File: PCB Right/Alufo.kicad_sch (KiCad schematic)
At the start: 32 parts, among them J2 USB_C_Receptacle_USB2.0_16P_2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, J4 USB_C_Receptacle_USB2.0_16P_2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, J6 SolderHole, SW2 BOOT, U2 CH552T, U4 USBLC6-2P6, U6 USBLC6-2P6

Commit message: Add cutout in middle layer for solder jump
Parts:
- J6: footprint TestPoint:TestPoint_THTPad_D2.5mm_Drill1.2mm -> Project Library:TestPoint_THTPad_D2.5mm_Drill1.2mm
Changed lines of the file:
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@@
 			)
 		)
-		(property "Footprint" "TestPoint:TestPoint_THTPad_D2.5mm_Drill1.2mm"
+		(property "Footprint" "Project Library:TestPoint_THTPad_D2.5mm_Drill1.2mm"
 			(at 165.1 157.48 0)
 			(effects

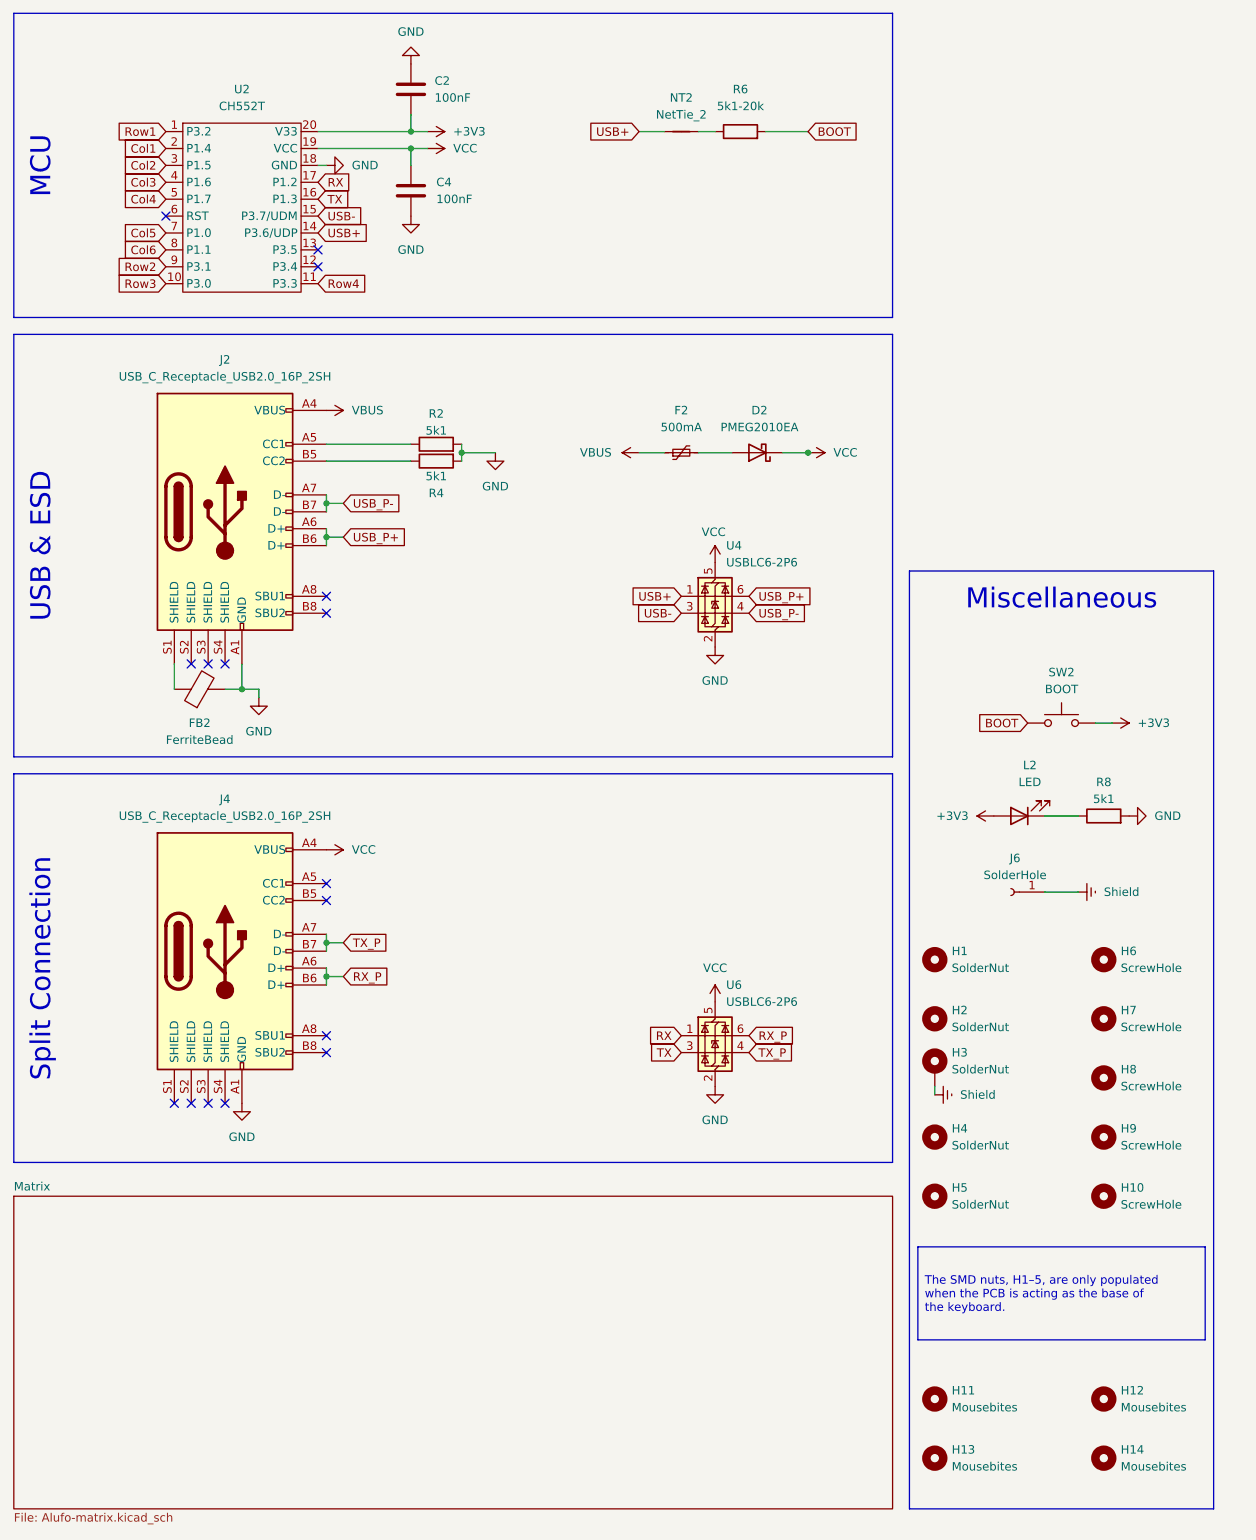
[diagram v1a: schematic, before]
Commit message: Update to KiCad v9
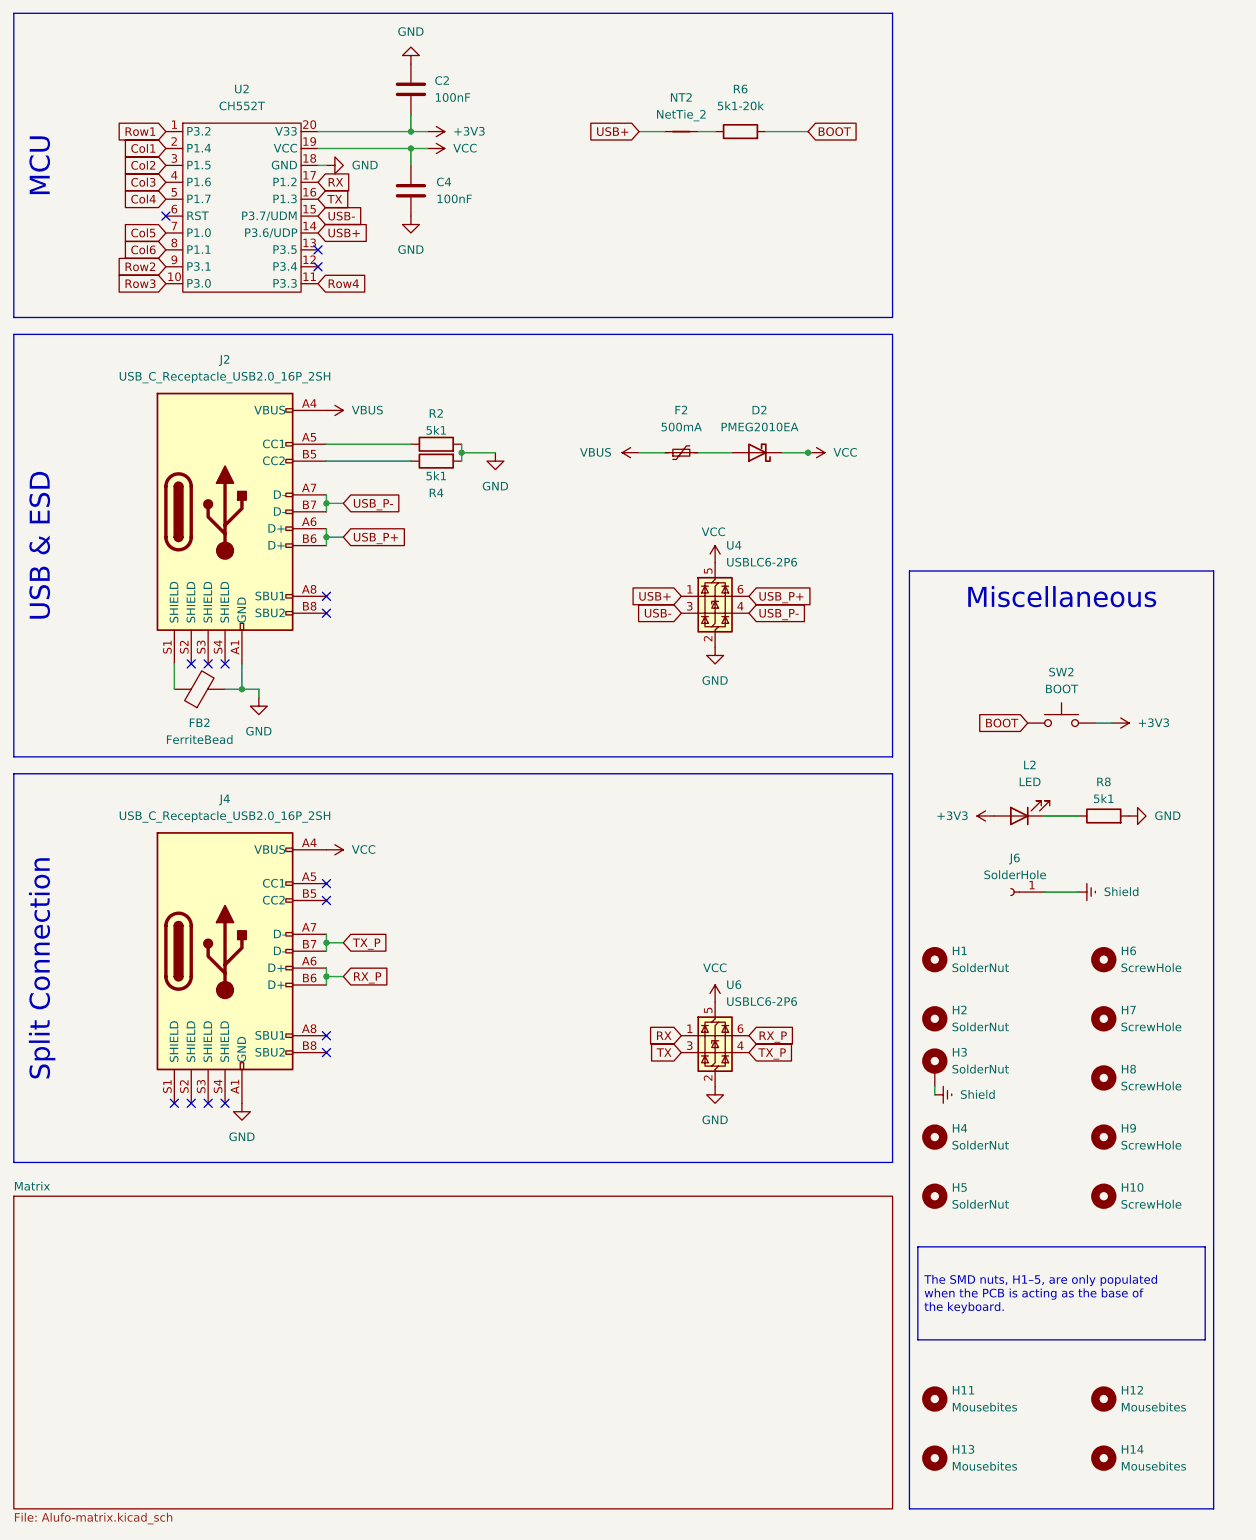
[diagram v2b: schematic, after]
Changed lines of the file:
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@@
 (kicad_sch
-	(version 20231120)
+	(version 20250114)
 	(generator "eeschema")
-	(generator_version "8.0")
+	(generator_version "9.0")
 	(paper "A4" portrait)
 	(title_block
@@
 		(comment 1 "Split one-layer reversible keyboard PCB (righthand side)")
 	)
+	(text_box "MCU"
+		(exclude_from_sim no)
+		(at 15.24 25.4 90)
+		(size 132.08 45.72)
+		(margins 2.25 2.25 2.25 2.25)
+		(stroke
+			(width 0)
+			(type default)
+		)
+		(fill
+			(type none)
+		)
+		(effects
+			(font
+				(size 3 3)
+			)
+			(justify top)
+		)
+	)
+	(text_box "Miscellaneous"
+		(exclude_from_sim no)
+		(at 149.86 109.22 0)
+		(size 45.72 140.97)
+		(margins 2.25 2.25 2.25 2.25)
+		(stroke
+			(width 0)
+			(type default)
+		)
+		(fill
+			(type none)
+		)
+		(effects
+			(font
+				(size 3 3)
+			)
+			(justify top)
+		)
+	)
+	(text_box "Split Connection"
+		(exclude_from_sim no)
+		(at 15.24 139.7 90)
+		(size 132.08 58.42)
+		(margins 2.25 2.25 2.25 2.25)
+		(stroke
+			(width 0)
+			(type default)
+		)
+		(fill
+			(type none)
+		)
+		(effects
+			(font
+				(size 3 3)
+			)
+			(justify top)
+		)
+	)
+	(text_box "USB & ESD"
+		(exclude_from_sim no)
+		(at 15.24 73.66 90)
+		(size 132.08 63.5)
+		(margins 2.25 2.25 2.25 2.25)
+		(stroke
+			(width 0)
+			(type default)
+		)
+		(fill
+			(type none)
+		)
+		(effects
+			(font
+				(size 3 3)
+			)
+			(justify top)
+		)
+	)
+	(text_box "The SMD nuts, H1–5, are only populated when the PCB is acting as the base of the keyboard."
+		(exclude_from_sim no)
+		(at 151.13 210.82 0)
+		(size 43.18 13.97)
+		(margins 0.9525 0.9525 0.9525 0.9525)
+		(stroke
+			(width 0)
+			(type default)
+		)
+		(fill
+			(type none)
+		)
+		(effects
+			(font
+				(size 1.27 1.27)
+			)
+			(justify left)
+		)
+	)
 	(junction
 		(at 49.53 127)
@@
 		)
 	)
-	(text_box "MCU"
-		(exclude_from_sim no)
-		(at 15.24 25.4 90)
-		(size 132.08 45.72)
-		(stroke
-			(width 0)
-			(type default)
-		)
-		(fill
-			(type none)
-		)
-		(effects
-			(font
-				(size 3 3)
-			)
-			(justify top)
-		)
-	)
-	(text_box "Miscellaneous"
-		(exclude_from_sim no)
-		(at 149.86 109.22 0)
-		(size 45.72 140.97)
-		(stroke
-			(width 0)
-			(type default)
-		)
-		(fill
-			(type none)
-		)
-		(effects
-			(font
-				(size 3 3)
-			)
-			(justify top)
-		)
-	)
-	(text_box "Split Connection"
-		(exclude_from_sim no)
-		(at 15.24 139.7 90)
-		(size 132.08 58.42)
-		(stroke
-			(width 0)
-			(type default)
-		)
-		(fill
-			(type none)
-		)
-		(effects
-			(font
-				(size 3 3)
-			)
-			(justify top)
-		)
-	)
-	(text_box "USB & ESD"
-		(exclude_from_sim no)
-		(at 15.24 73.66 90)
-		(size 132.08 63.5)
-		(stroke
-			(width 0)
-			(type default)
-		)
-		(fill
-			(type none)
-		)
-		(effects
-			(font
-				(size 3 3)
-			)
-			(justify top)
-		)
-	)
-	(text_box "The SMD nuts, H1–5, are only populated when the PCB is acting as the base of the keyboard."
-		(exclude_from_sim no)
-		(at 151.13 210.82 0)
-		(size 43.18 13.97)
-		(stroke
-			(width 0)
-			(type default)
-		)
-		(fill
-			(type none)
-		)
-		(effects
-			(font
-				(size 1.27 1.27)
-			)
-			(justify left)
-		)
-	)
 	(global_label "USB-"
 		(shape input)
@@
 		(at 15.24 203.2)
 		(size 132.08 46.99)
+		(exclude_from_sim no)
+		(in_bom yes)
+		(on_board yes)
+		(dnp no)
 		(fields_autoplaced yes)
 		(stroke
@@
 		)
 	)
+	(embedded_fonts no)
 )

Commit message: Further library name corrections in schematic; update PCB
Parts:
- H1, H2, H4, H5: footprint Project Library:MountingHole_2.2mm_M2_SMD_Solder_Nut -> Project_Library:MountingHole_2.2mm_M2_SMD_Solder_Nut
- H11, H12, H13, H14: footprint Project Library:Mousebites -> Project_Library:Mousebites
- H3: footprint Project Library:MountingHole_2.2mm_M2_SMD_Solder_Nut_Pad -> Project_Library:MountingHole_2.2mm_M2_SMD_Solder_Nut_Pad
- J2, J4: footprint Project Library:USB_C_Receptacle_HRO_TYPE-C-31-M-12 -> Project_Library:USB_C_Receptacle_HRO_TYPE-C-31-M-12; symbol Project Library:USB_C_Receptacle_USB2.0_16P_2SH -> Project_Library:USB_C_Receptacle_USB2.0_16P_2SH
- J6: footprint Project Library:TestPoint_THTPad_D2.5mm_Drill1.2mm -> Project_Library:TestPoint_THTPad_D2.5mm_Drill1.2mm
- L2: footprint Project Library:LED_0805_2012Metric_Mod -> Project_Library:LED_0805_2012Metric_Mod
- NT2: footprint Project Library:NetTie-2_SMD_Pad0.2mm -> Project_Library:NetTie-2_SMD_Pad0.2mm
- SW2: footprint Project Library:SW_SPST_SKQG_WithStem -> Project_Library:SW_SPST_SKQG_WithStem
- U2: symbol Project Library:MCU_CH552T_TSSOP-20 -> Project_Library:MCU_CH552T_TSSOP-20
- U4, U6: footprint Project Library:SOT-666_Mod -> Project_Library:SOT-666_Mod
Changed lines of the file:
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@@
 	)
 	(symbol
-		(lib_id "Project Library:USB_C_Receptacle_USB2.0_16P_2SH")
+		(lib_id "Project_Library:USB_C_Receptacle_USB2.0_16P_2SH")
 		(at 46.99 100.33 0)
 		(unit 1)
@@
 			)
 		)
-		(property "Footprint" "Project Library:USB_C_Receptacle_HRO_TYPE-C-31-M-12"
+		(property "Footprint" "Project_Library:USB_C_Receptacle_HRO_TYPE-C-31-M-12"
 			(at 50.8 100.33 0)
 			(effects
@@
 			)
 		)
-		(property "Footprint" "Project Library:Mousebites"
+		(property "Footprint" "Project_Library:Mousebites"
 			(at 179.07 233.68 0)
 			(effects
@@
 	)
 	(symbol
-		(lib_id "Project Library:USB_C_Receptacle_USB2.0_16P_2SH")
+		(lib_id "Project_Library:USB_C_Receptacle_USB2.0_16P_2SH")
 		(at 46.99 166.37 0)
 		(unit 1)
@@
 			)
 		)
-		(property "Footprint" "Project Library:USB_C_Receptacle_HRO_TYPE-C-31-M-12"
+		(property "Footprint" "Project_Library:USB_C_Receptacle_HRO_TYPE-C-31-M-12"
 			(at 50.8 166.37 0)
 			(effects
@@
 			)
 		)
-		(property "Footprint" "Project Library:SOT-666_Mod"
+		(property "Footprint" "Project_Library:SOT-666_Mod"
 			(at 121.666 185.801 0)
 			(effects
@@
 			)
 		)
-		(property "Footprint" "Project Library:LED_0805_2012Metric_Mod"
+		(property "Footprint" "Project_Library:LED_0805_2012Metric_Mod"
 			(at 166.37 146.05 0)
 			(effects
@@
 			)
 		)
-		(property "Footprint" "Project Library:Mousebites"
+		(property "Footprint" "Project_Library:Mousebites"
 			(at 179.07 242.57 0)
 			(effects
@@
 			)
 		)
-		(property "Footprint" "Project Library:MountingHole_2.2mm_M2_SMD_Solder_Nut"
+		(property "Footprint" "Project_Library:MountingHole_2.2mm_M2_SMD_Solder_Nut"
 			(at 153.67 203.2 0)
 			(effects
@@
 			)
 		)
-		(property "Footprint" "Project Library:TestPoint_THTPad_D2.5mm_Drill1.2mm"
+		(property "Footprint" "Project_Library:TestPoint_THTPad_D2.5mm_Drill1.2mm"
 			(at 165.1 157.48 0)
 			(effects
@@
 			)
 		)
-		(property "Footprint" "Project Library:Mousebites"
+		(property "Footprint" "Project_Library:Mousebites"
 			(at 153.67 233.68 0)
 			(effects
@@
 			)
 		)
-		(property "Footprint" "Project Library:MountingHole_2.2mm_M2_SMD_Solder_Nut"
+		(property "Footprint" "Project_Library:MountingHole_2.2mm_M2_SMD_Solder_Nut"
 			(at 153.67 167.64 0)
 			(effects
@@
 			)
 		)
-		(property "Footprint" "Project Library:MountingHole_2.2mm_M2_SMD_Solder_Nut"
+		(property "Footprint" "Project_Library:MountingHole_2.2mm_M2_SMD_Solder_Nut"
 			(at 153.67 194.31 0)
 			(effects
@@
 			)
 		)
-		(property "Footprint" "Project Library:Mousebites"
+		(property "Footprint" "Project_Library:Mousebites"
 			(at 153.67 242.57 0)
 			(effects
@@
 			)
 		)
-		(property "Footprint" "Project Library:SOT-666_Mod"
+		(property "Footprint" "Project_Library:SOT-666_Mod"
 			(at 121.666 119.761 0)
 			(effects
@@
 			)
 		)
-		(property "Footprint" "Project Library:MountingHole_2.2mm_M2_SMD_Solder_Nut_Pad"
+		(property "Footprint" "Project_Library:MountingHole_2.2mm_M2_SMD_Solder_Nut_Pad"
 			(at 153.67 184.15 0)
 			(effects
@@
 	)
 	(symbol
-		(lib_id "Project Library:MCU_CH552T_TSSOP-20")
+		(lib_id "Project_Library:MCU_CH552T_TSSOP-20")
 		(at 49.53 52.07 0)
 		(unit 1)
@@
 			)
 		)
-		(property "Footprint" "Project Library:NetTie-2_SMD_Pad0.2mm"
+		(property "Footprint" "Project_Library:NetTie-2_SMD_Pad0.2mm"
 			(at 115.57 43.18 0)
 			(effects
@@
 			)
 		)
-		(property "Footprint" "Project Library:SW_SPST_SKQG_WithStem"
+		(property "Footprint" "Project_Library:SW_SPST_SKQG_WithStem"
 			(at 172.72 127 0)
 			(effects
@@
 			)
 		)
-		(property "Footprint" "Project Library:MountingHole_2.2mm_M2_SMD_Solder_Nut"
+		(property "Footprint" "Project_Library:MountingHole_2.2mm_M2_SMD_Solder_Nut"
 			(at 153.67 176.53 0)
 			(effects
